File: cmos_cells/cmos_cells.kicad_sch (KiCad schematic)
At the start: 448 parts, among them P1 PMOS, P10 PMOS, P11 PMOS, P12 PMOS, P13 PMOS, P2 PMOS, P3 PMOS, P4 PMOS, P5 PMOS, P6 PMOS, P7 PMOS, P8 PMOS, P9 PMOS

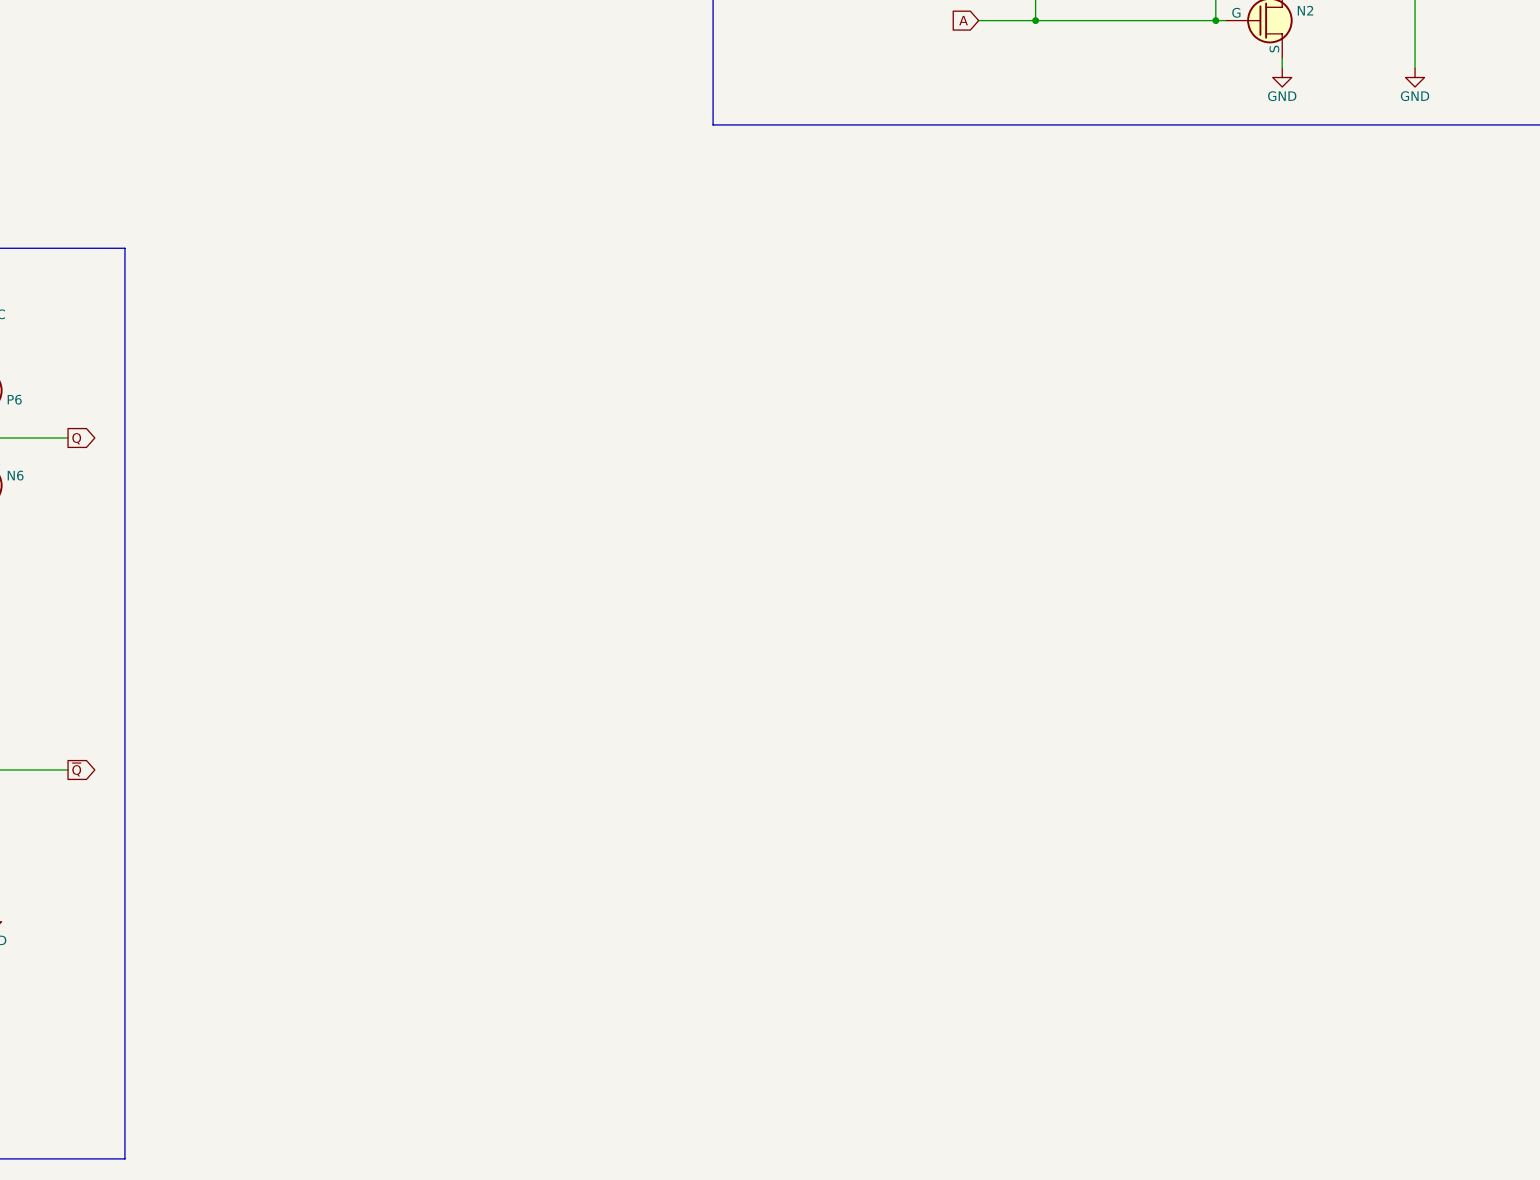
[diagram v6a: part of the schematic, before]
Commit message: Add layout and schematic for tri-state buffer cell
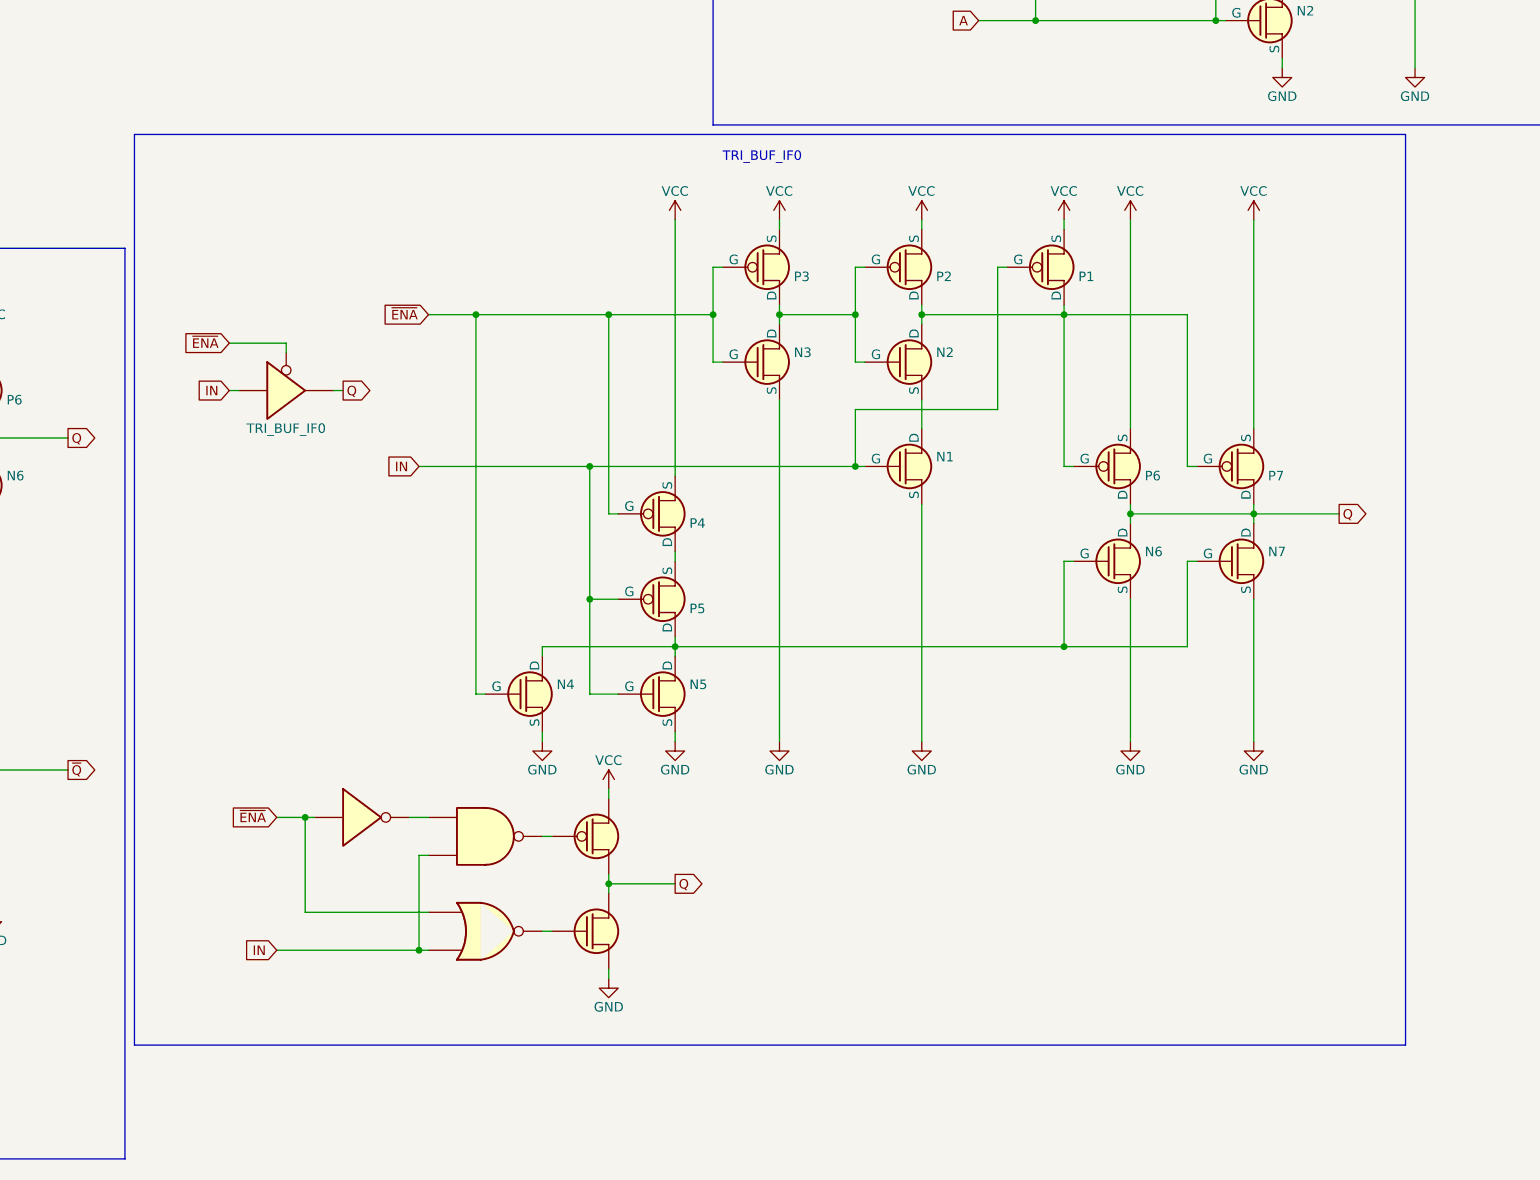
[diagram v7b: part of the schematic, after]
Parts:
- added N1, N2, N3, N4, N5, N6, N7, N?: NMOS, symbol DMG_CPU_Cells:NMOS
- added P1, P2, P3, P4, P5, P6, P7, P?: PMOS, symbol DMG_CPU_Cells:PMOS
- added U?: INVERTER_A, symbol DMG_CPU_Cells:INVERTER_A
- added U?: TRI_BUF_IF0, symbol DMG_CPU_Cells:TRI_BUF_IF0
- added U?: NAND_2, symbol DMG_CPU_Cells:NAND_2
- added U?: NOR_2, symbol DMG_CPU_Cells:NOR_2
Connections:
- net GND: now also N1.3 (S), N3.3 (S), N4.3 (S), N5.3 (S), N6.3 (S), N7.3 (S), N?.3 (S)
- net IN: now also N1.2 (G), N5.2 (G), P1.2 (G), P5.2 (G), U?.1 (IN), U?.2, U?.2, U?.3 (IN)
- net Q: now also N6.1 (D), N7.1 (D), N?.1 (D), P6.1 (D), P7.1 (D), P?.1 (D), U?.4
- net VCC: now also P1.3 (S), P2.3 (S), P3.3 (S), P4.3 (S), P6.3 (S), P7.3 (S), P?.3 (S)
- net ~{ENA}: now also N3.2 (G), N4.2 (G), P3.2 (G), P4.2 (G), U?.1, U?.1, U?.2 (~{ENA})
- new net: N2.2 (G), N3.1 (D), P2.2 (G), P3.1 (D)
- new net: N2.1 (D), P1.1 (D), P2.1 (D), P6.2 (G), P7.2 (G)
- new net: N1.1 (D), N2.3 (S)
- new net: N?.2 (G), U?.3
- new net: U?.1, U?.2
- new net: P?.2 (G), U?.3
- new net: N4.1 (D), N5.1 (D), N6.2 (G), N7.2 (G), P5.1 (D)
- new net: P4.1 (D), P5.3 (S)
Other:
- note added: "TRI_BUF_IF0"

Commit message: Add schematics for IO pads
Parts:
- added D1 (x7), D2 (x7), D3, D4: D, symbol Device:D
- added N1 (x6), N2 (x5), N3, N4: NMOS, symbol DMG_CPU_Cells:NMOS
- added P1 (x7), P2 (x4), P3 (x4), P4: PMOS, symbol DMG_CPU_Cells:PMOS
- added R1 (x3): 25k, symbol Device:R
- added TP? (x2): XI, symbol Connector:TestPoint
- added TP? (x6): Bonding Pad, symbol Connector:TestPoint
- added TP? (x2): XO, symbol Connector:TestPoint
- added U?: OBUF_A, symbol DMG_CPU_Cells:OBUF_A
- added U? (x2): INVERTER_A, symbol DMG_CPU_Cells:INVERTER_A
- added U?: OBUF_B, symbol DMG_CPU_Cells:OBUF_B
- added U?: IBUF, symbol DMG_CPU_Cells:IBUF
- added U?: IOBUF_A, symbol DMG_CPU_Cells:IOBUF_A
- added U?: IOBUF_C, symbol DMG_CPU_Cells:IOBUF_C
- added U?: NAND_2, symbol DMG_CPU_Cells:NAND_2
- added U?: OSC, symbol DMG_CPU_Cells:OSC
- added U?: IOBUF_B, symbol DMG_CPU_Cells:IOBUF_B
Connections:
- net ENA: now also N2.2 (G), P2.2 (G), U?.1, U?.2 (ENA)
- net GND: now also D2.2 (A), D2.2 (A), D2.2 (A), D2.2 (A), D2.2 (A), D2.2 (A), D2.2 (A), D4.2 (A), N1.3 (S), N1.3 (S), N1.3 (S), N1.3 (S), N1.3 (S), N2.3 (S), N2.3 (S), N2.3 (S), N2.3 (S), N2.3 (S), N3.3 (S), N4.3 (S)
- net VCC: now also D1.1 (K), D1.1 (K), D1.1 (K), D1.1 (K), D1.1 (K), D1.1 (K), D1.1 (K), D3.1 (K), P1.3 (S), P1.3 (S), P1.3 (S), P1.3 (S), P1.3 (S), P1.3 (S), P1.3 (S), P2.3 (S), P2.3 (S), P2.3 (S), P2.3 (S), P3.3 (S), P4.3 (S), R1.1, R1.1, R1.1
- new net: D1.2 (A), D2.1 (K), N1.1 (D), P1.1 (D), TP?.1 (x2)
- new net: D3.2 (A), D4.1 (K), N4.2 (G), P4.2 (G), TP?.1
- new net: N1.1 (D), N3.2 (G), P1.1 (D), P2.1 (D), P3.2 (G)
- new net: D1.2 (A), D2.1 (K), N1.1 (D), N2.2 (G), P1.1 (D), P2.2 (G), P3.1 (D), TP?.1 (x2)
- new net: D1.2 (A), D2.1 (K), N2.1 (D), N2.2 (G), P1.1 (D), P2.2 (G), P3.1 (D), TP?.1
- new net: TP?.1, U?.1
- new net: N1.3 (S), N2.1 (D)
- new net: P3.3 (S), R1.2 (x3)
- new net: D1.2 (A), D2.1 (K), N3.1 (D), P3.1 (D), TP?.1
- new net: D1.2 (A), D2.1 (K), N1.2 (G), P1.2 (G), TP?.1
- new net: U?.1, U?.3
- new net: TP?.1, U?.2
- new net DRV_LOW: N1.2 (G), N1.2 (G), N1.2 (G), N2.2 (G), P3.2 (G), U?.1 (DRV_LOW), U?.1 (DRV_LOW), U?.1 (DRV_LOW), U?.1 (DRV_LOW)
- new net ~{CLK}: N1.2 (G), N4.1 (D), P1.2 (G), P4.1 (D), U?.1 (CLK), U?.2, U?.2
- new net ~{DRV}_HIGH: P1.2 (G), P1.2 (G), P1.2 (G), P1.2 (G), U?.2 (~{DRV}_HIGH), U?.3 (~{DRV}_HIGH), U?.4 (~{DRV}_HIGH), U?.4 (~{DRV}_HIGH)
- new net ~{ENA}_PU: P3.2 (G), P3.2 (G), U?.3 (~{ENA}_PU), U?.3 (~{ENA}_PU)
- new net ~{INPUT}: N1.1 (D), N2.1 (D), N2.1 (D), N2.1 (D), P1.1 (D), P2.1 (D), P2.1 (D), P2.1 (D), U?.1 (~{INPUT}), U?.2 (~{INPUT}), U?.2 (~{INPUT}), U?.2 (~{INPUT})
- new net ~{OUTPUT}: N1.2 (G), P1.2 (G), U?.1 (~{OUTPUT})
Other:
- note added: "IBUF"
- note added: "IOBUF_A"
- note added: "IOBUF_B"
- note added: "IOBUF_C"
- note added: "OBUF_A"
- note added: "OBUF_B"
- note added: "OSC"
